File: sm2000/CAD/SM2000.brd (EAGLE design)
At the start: 160 x 100 mm, 365 parts, among them CN1 HDR100-3, CN10 ST-3509, CN11 HDR100-3, CN2 JS-MU3-002, CN3 DS-0518, CN5 ST-3509, CN8 ST-3509, J1 JMP-2PIN, J2 JMP-2PIN, J3 JMP-2PIN, J4 CONN-BOOM-XH-2A, P10 TPAD50, P11 TPAD50, P12 TPAD50, P13 TPAD50, P14 TPAD50, P16 TPAD50, P18 TPAD50, P19 TPAD50, P20 TPAD50, P21 TPAD50, P3 TPAD50, P4 TPAD50, P5 TPAD50, P6 TPAD50, P7 TPAD50, P8 TPAD50, P9 TPAD50, Q1 MMBT3904, Q10 MMBT3904, Q11 STR2P3LLH6, Q12 BRF92, Q13 BFQ19, Q14 RD01MUS2, Q15 MMBT3904, Q17 MMBT3904, Q18 MMBT3904, Q2 MMBT3904, Q3 MMBT3904, Q4 MMBT3904, Q5 MMBT3904, Q6 MMBT3904, Q7 BC548, Q8 BC549, Q9 STR2P3LLH6, SW1 SW-LC2259, SW2 TS-026, SW3 SW-LC2259EENP, SW4 TS-026, SW5 TS-02B, U1 STM32F405VGT6, U10 DNL, U11 L78MXX, U12 PGA-103+, U13 ADE-1, U14 SI570, U15 SI5351A, U2 L78MXX, U3 STMPS2141, U4 EMIF02-USB03F2, U5 L78MXX, U6 LD3985M33R, U7 SA612A, U8 LM386M-1, U9 LMV341, X1 BU-SMA-H, X2 BU-SMA-H

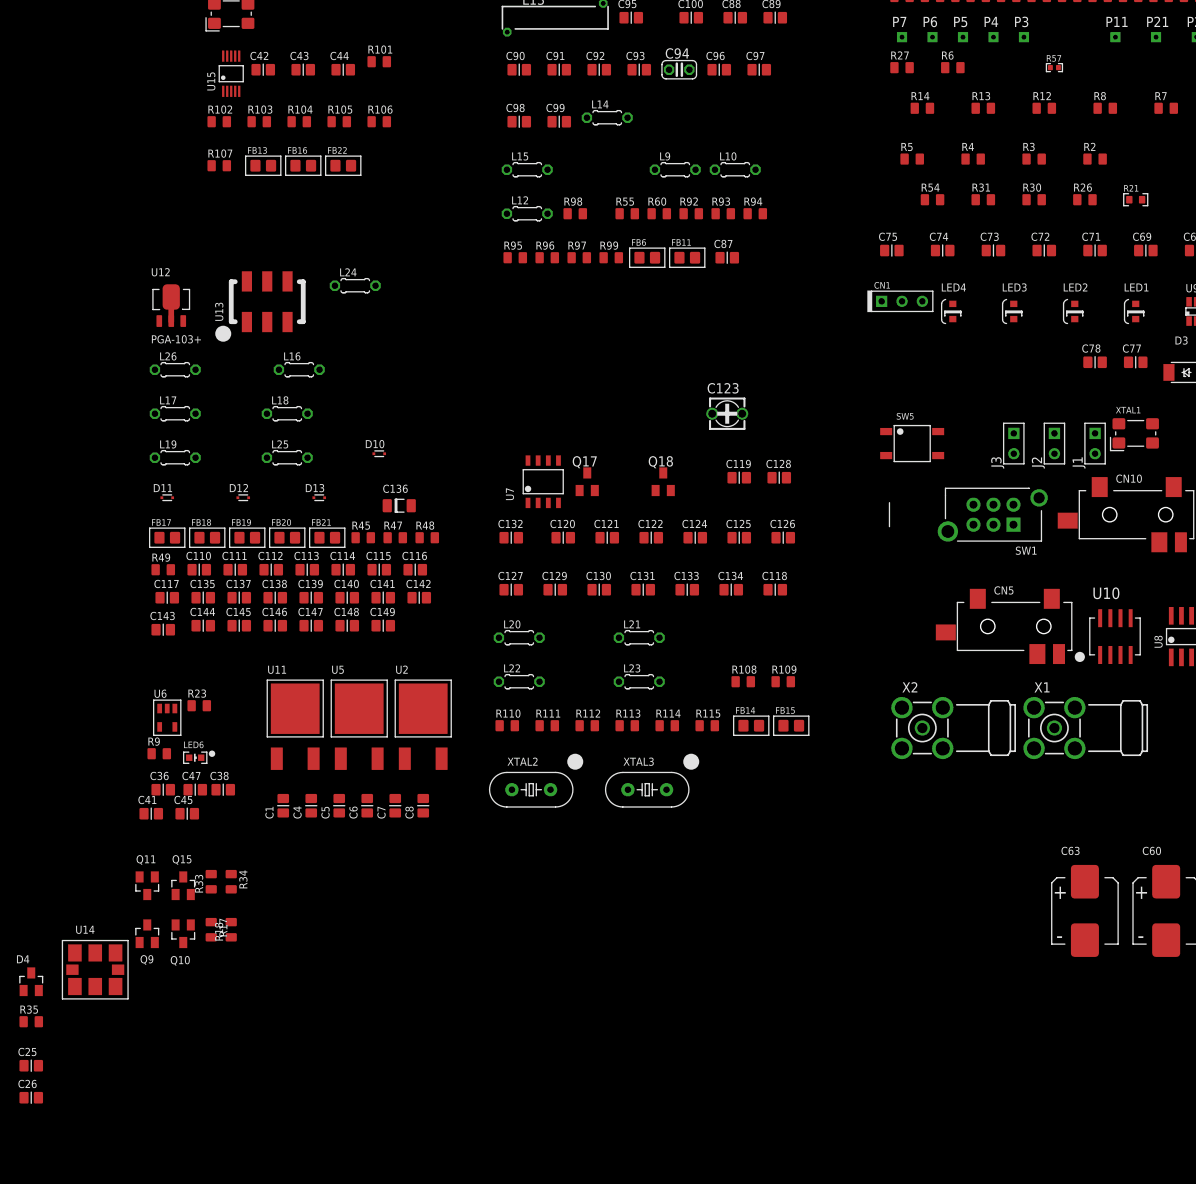
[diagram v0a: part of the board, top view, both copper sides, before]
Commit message: Intermediate update: Fix resistor tolerances fix cap working voltages Fix some library items for no name & no value email Schematic Updates 01/01/2016 item 1. email Commits to SVN 01/02/2016 items 1, i,ii,iii,iv, 2,3,4 RGB
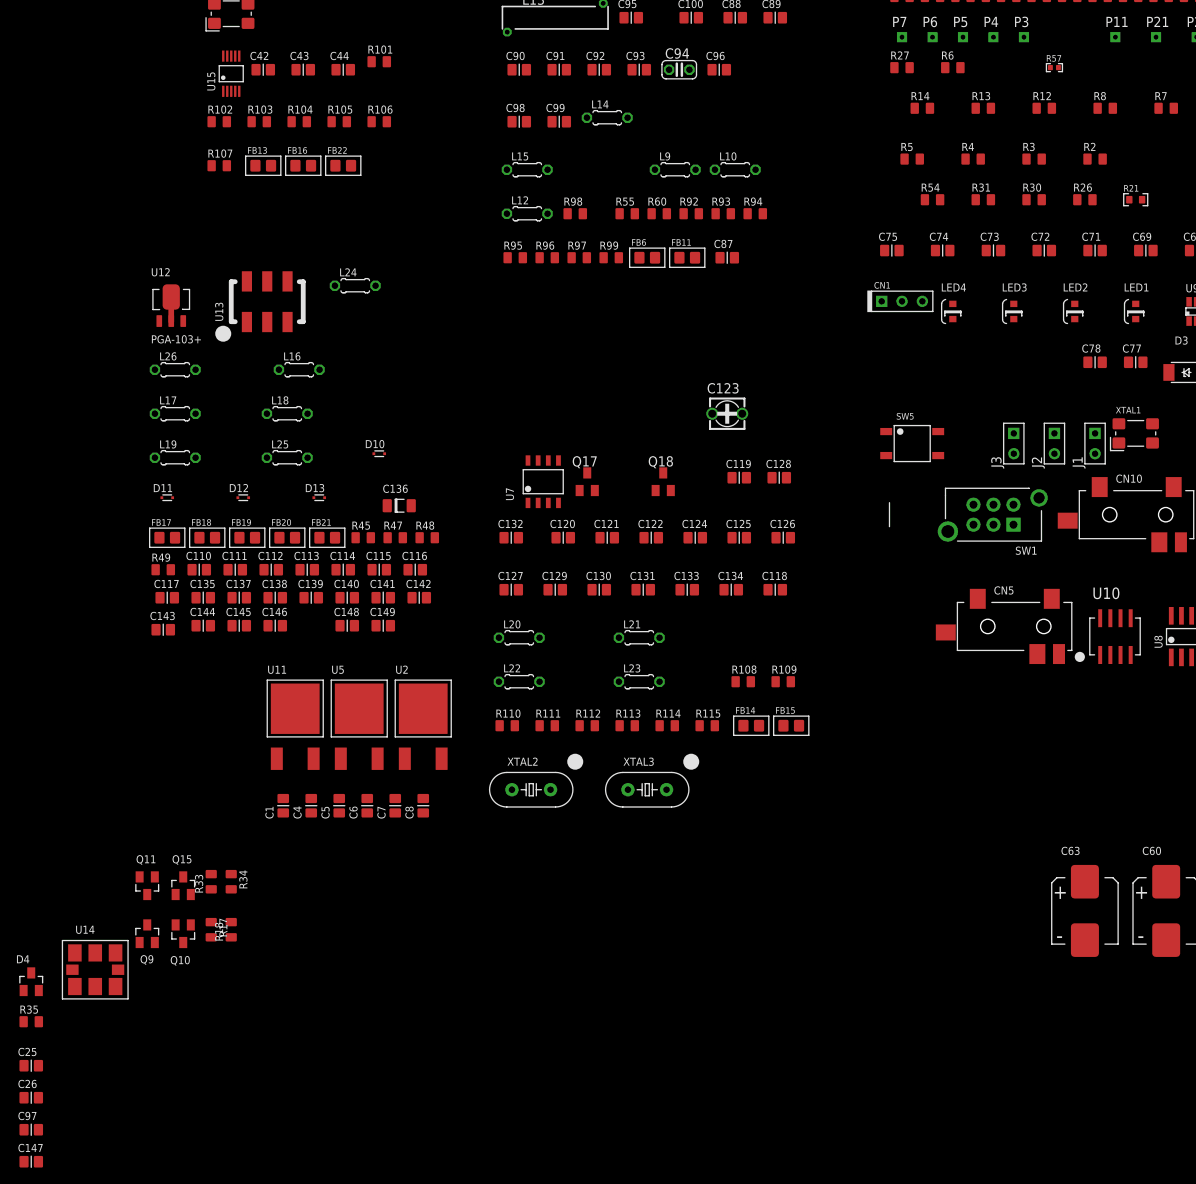
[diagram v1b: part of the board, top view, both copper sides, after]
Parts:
- removed C36, C47: 1uF,16V, _RoweTel:C0805
- removed C38: 10nF,25V, _RoweTel:C0805
- removed C41, C45: 100nF,25V, _RoweTel:C0805
- removed LED6: DNL, _RoweTel:SML-LX0603SRW
- removed R23: 0 Ohm, _RoweTel:R0805
- removed R9: DNL, _RoweTel:R0805
- removed U6: LD3985M33R, _RoweTel:SOT23-5L
- removed X1, X2: BU-SMA-H, _RoweTel:BU-SMA-H
- C100, C93: value 33p -> 33pF,50V
- C110: value 12p -> 12pF.50V
- C111, C112, C139, C140: value 3p3 -> 3.3pF,50V
- C113, C138, C141: value 12p -> 12pF,50V
- C114, C142: value 0.5p -> 0.5pF,50V
- C115, C116, C117, C130, C133, C134, C135, C137, C147, C148, C149, C88, C90, C96, C98: value 1n -> 1nF,25V
- C118, C121, C124, C125, C126, C131, C78: value 0.1u -> 0.1uF,25V
- C120: value 39pF -> 39pF,50V
- C122, C89: value 5p6 -> 5.6pF,50V
- C127: value 27pF -> 27pF,50V
- C128, C132: value 150pF -> 150pF,50V
- C129, C91, C92, C97: value 0.1u -> 0.1uF.25V
- C136: value 1u -> 1uF,25V
- C143, C144: value 2p2 -> 2.2pF,50V
- C145, C94: value 22p -> 22pF,50V
- C146: value 22p -> 22pF,25V
- C25: value (none) -> 1pF,50V
- C26: value (none) -> 1nF,25V
- C28: value 100nF -> 100nF,25V
- C87: value 22pF -> 22pF,50V
- C95: value 1n DNL -> 1nF,25V
- C99: value 47p -> 47pF,50V
- L14, L15: value 57nH air core 4T 2mm ID -> 57nH
- L16, L17, L18, L19: value 68nH 4.5T 5mm ID -> 68nH
- L24: value 260nH 8T 6.25mm ID -> 260nH
- L26: value 220nH 7T 6.25mm ID -> 220nH
- Q7: value BC548 -> MMBT3904
- Q8: value BC549 -> MMBT3906
- R101, R104, R115, R92: value 150 -> 150,1%
- R102, R103, R109, R113, R84, R94: value 1k -> 1K,1%
- R105, R106, R107: value 0R -> 0 Ohm
- R108, R60, R93: value 3k -> 3K,1%
- R110, R70, R80, R86, R87, R96, R97: value 10 -> 10,1%
- R111: value 33k -> 33K,1%
- R112: value 15k -> 15K,1%
- R114: value 50 -> 50,1%
- R35: value RES-0805 -> 330,1%
- R45, R47, R83: value 18k -> 18K,1%
- R48: value 68k -> 68K,1%
- R49, R88: value 2k2 -> 2.2K,1%
- R55: value 10k -> 10K,1%
- R59, R72: value 330 -> 330,1%
- R63, R73: value 680 -> 680,1%
- R64, R74: value 10K -> 10K,1%
- R65, R68, R75, R78: value 2.2K -> 2.2K,1%
- R66, R76: value 180 -> 180,1%
- R67, R77: value 15 -> 15,1%
- R69, R79: value 470 -> 470,1%
- R71, R81: value 47 -> 47,1%
- R82: value 39k -> 39K,1%
- R85, R91: value 3k3 -> 3.3K,1%
- R89, R90: value 100 -> 100,1%
- R95: value 50 -> 49.4,1%
- R98: value 47 DNL -> 47,1%, DNL
- R99: value 4k7 -> 4.7K,1%
- moved C97 160.7 mm to (-228.0, -38.0)
- moved C147 75.6 mm to (-228.0, -42.0)
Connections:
- net N$38 renamed DRIVER/PA_INPUT
- removed net N$100: C71.2, C75.1, X1.1
- removed net N$37 (its old number): C38.1, U6.4
- removed net N$40: Q11.3, R80.1
- removed net N$52: LED6.A, R9.1
- removed net N$56: L20.1
- removed net N$79: L11.2, L13.2, R97.1
- removed net N$90: C69.1, C76.2, X2.1
- new net N$19: L13.1, R97.1
- new net PA_OUTPUT: C149.2
- new net RX+12V: Q9.3, R70.2
- new net TIAIN: C71.2, C75.1, U13.5
- new net TIAOUT: C69.1, C76.2, L20.1
- new net TX+12V: L11.2, Q11.3, R47.1, R49.2, R80.1
- net +12V: no longer Q11.2, Q9.2, R17.2, R33.2
- net +12V_RX: now also R45.1; no longer Q9.3, R70.2
- net +3.3V: no longer C36.1, C41.1, R23.1, R9.2, U6.5
- net +5V: no longer C45.1, C47.1, U6.1, U6.3
- net +9V: now also L13.2; no longer L13.1
- net +VIN: now also Q11.2, Q9.2, R17.2, R33.2
- net GND: no longer C36.2, C38.2, C41.2, C45.2, C47.2, LED6.C, U6.2, X1.2, X1.3, X1.4, X1.5, X2.2, X2.3, X2.4, X2.5
- net VDD: no longer R23.2

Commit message: Update schematic. Moved new component footprints onto PCB Matched schematic to emailchange lists. reorganized circuitry blocks on pages. RGB
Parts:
- added C27: 1nF,25V, _RoweTel:C0805
- added J10, J11, J12, J5, J6, J7, J8, J9: JMPR-2X2, _RoweTel:JMPR-2X2X.1
- added SH4, SH5: SHUNT, _RoweTel:SHUNT
- C119, C80, C81: value 10uF -> 10uF,25V,EL; device _RoweTel:C0805 -> _RoweTel:NICHICON-WJ-5
- C79, C82: value 10uF tant -> 10uF,25V,EL; device _RoweTel:C0805 -> _RoweTel:NICHICON-WJ-5
- R114: value 50,1% -> 49.9,1%
- R95: value 49.4,1% -> 49.9,1%
- moved U14 243.5 mm to (12.0, 56.0)
- moved L19 241.6 mm to (31.5, 53.5)
- moved L17 241.6 mm to (31.5, 57.0)
- moved L26 241.5 mm to (31.5, 60.5)
- moved L25 235.1 mm to (39.0, 53.5)
- moved L18 235.1 mm to (39.0, 57.0)
- moved L16 233.5 mm to (39.0, 60.5)
- moved Q14 224.5 mm to (39.0, 19.0)
- moved L24 219.0 mm to (31.5, 64.0)
- moved XTAL5 215.2 mm to (11.0, 79.0)
- moved U13 210.0 mm to (11.5, 68.5)
- moved L15 205.5 mm to (39.0, 67.5)
- moved L12 205.4 mm to (39.0, 64.0)
- moved U11 204.6 mm to (9.50, 17.0)
- moved U2 204.6 mm to (25.5, 17.0)
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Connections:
- net +12V_RX_ENB renamed +12VRXENB
- removed net N$127: C111.2, U13.3
- new net N$40: C126.2, J6.1
- new net N$52: C100.1, J9.1, L14.2
- new net N$56: C111.2, J12.2
- new net N$58: J12.1, U13.3
- new net N$59: C27.2, J10.1
- new net N$61: C27.1, U12.1
- new net N$63: J8.1
- new net N$79: C112.1, J11.1
- new net TIA_OUT: C69.1, C76.2, J5.1, L20.1
- net ANT_SMA: now also J9.2; no longer C100.1, L14.2
- net BBAMP: now also J7.1
- net GND: now also J10.3, J10.4, J11.3, J11.4, J12.3, J12.4, J5.3, J5.4, J6.3, J6.4, J7.3, J7.4, J8.3, J8.4, J9.3, J9.4
- net N$104: now also J7.2
- net N$11: now also J10.2; no longer U12.1
- net N$112: now also J8.2
- net N$135: now also J11.2; no longer C112.1
- net N$49: now also J6.2; no longer C126.2
- net TIAOUT: now also J5.2; no longer C69.1, C76.2, L20.1

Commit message: Implemented changes from D. Rowes email: Comments #1 RGB
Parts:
- removed C64: 22uF,25V, _RoweTel:C0805
- removed C66: 100nF,25V, _RoweTel:C0805
- removed U5: L78MXX, _RoweTel:DPAK
- added C101: 10nF,25V, _RoweTel:C0805
- added C103, C164: 100nF,25V, _RoweTel:C0805
- added C107: 100nF,25V, AA-ipc-7351-capacitor:CAPC1005X60N
- added C108: 20pF,50V, AA-ipc-7351-capacitor:CAPC1005X60N
- added C109: 8.2nF,25V, ipc-7351-capacitor:CAPC1608X92N
- added C150, C179: 22uF,25V, _RoweTel:C1210
- added C166: 470nF,25V, ipc-7351-capacitor:CAPC1608X92N
- added C167: 22uF,25V,1210, AA-ipc-7351-capacitor:CAPC3225X168N
- added C29, C31: CAP-10UF-WJ5, _RoweTel:NICHICON-WJ-5
- added C36: 1nF,25V, _RoweTel:C0805
- added J13: JMPR-2X2, _RoweTel:JMPR-2X2X.1
- added L1: 4.2uH, _RoweTel:SRR5028
- added R127: 124.0K,1%, AA-ipc-7351-resistor:RESC1005X40AN
- added R128: 22.1K,1%, AA-ipc-7351-resistor:RESC1005X40AN
- added R129: 10K,1%, AA-ipc-7351-resistor:RESC1005X40AN
- added U$16: (no value), _RoweTel:SWPS-OTL
- added U17: TPS54329E, _RoweTel:PSO-DDA
- added U6: LD3985M33R, _RoweTel:SOT23-5L
- C1: value .33uF,25V -> 100nF,25V
- C5, C7: value .33uF,25V -> CAP-10UF-WJ5; device _RoweTel:C0805 -> _RoweTel:NICHICON-WJ-5
- C65: value 1uF,16V -> 1uF,25V
- moved C1 247.8 mm to (50.0, -23.0), turned to 0 degrees
- moved C147 44.6 mm to (-224.5, 2.50)
- moved C25 44.6 mm to (-224.5, 14.5)
- moved C26 44.6 mm to (-224.5, 10.5)
- moved C97 44.6 mm to (-224.5, 6.50)
- moved D4 44.6 mm to (-224.5, 25.0)
- moved R35 44.6 mm to (-224.5, 20.0)
- moved C27 23.3 mm to (-224.5, -1.50)
- moved C7 21.8 mm to (-201.0, 14.0), turned to 0 degrees
- moved C5 12.3 mm to (-185.0, 14.0), turned to 0 degrees
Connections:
- removed net N$63: J8.1
- new net N$127: C101.1, U6.4
- new net N$169: C107.1, U17.1
- new net N$170: C108.2, R127.2, R128.1, U17.5
- new net N$171: C109.1, U17.8
- new net N$172: C166.1, U17.6
- new net N$173: R129.2, U17.7
- new net N$222: C150.1, C164.1, C179.1, C36.1, R129.1, R21.2, U17.2
- new net N$90: J13.2, U13.5
- new net SW: C107.2, L1.1, U17.3
- net +3.3V: now also C8.1, U11.3
- net +5V: now also C108.1, C167.1, C7.1, FB8.1, L1.2, R127.1, U11.1; no longer C6.1, U5.3
- net +9V: now also L11.2; no longer L13.2
- net +VIN: now also C31.1, U2.1
- net AVDD: now also C5.1, C6.1, FB7.1, U6.5; no longer C64.1, C66.1, FB8.2
- net GND: now also C101.2, C103.2, C109.2, C150.2, C164.2, C166.2, C167.2, C179.2, C29.2, C31.2, C36.2, J13.3, J13.4, R128.2, U17.4, U17.EP, U6.2; no longer C64.2, C66.2, U5.4
- net N$144: now also XTAL3.2; no longer XTAL3.1
- net N$145: now also XTAL3.1; no longer XTAL3.2
- net N$54: now also C103.1, C29.1, FB8.2, U6.1, U6.3; no longer C5.1, C7.1, R21.2, U11.1, U2.1, U5.1
- net TIAIN: now also J13.1; no longer U13.5
- net TX+12V: now also L13.2; no longer L11.2
- net VDD: no longer C8.1, FB7.1, FB8.1, U11.3
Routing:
- added copper zone on layer 15, net AVDD
- added copper zone on layer 2, net GND
- added copper zone on layer 15, net VDD
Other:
- board text added: "L2-GND"
- board text added: "L3-VDD-AVDD"

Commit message: Changes to schematics per emails of 1/12/2016 - 1/14/2016 per David Rowe.
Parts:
- removed C101: 10nF,25V, _RoweTel:C0805
- removed P5, P6, P7, P8: TPAD50, _Coherix:TPAD50
- removed U$16: (no value), _RoweTel:SWPS-OTL
- added C38: 100uF,25V,EL, _RoweTel:CAP-CHEMI-F80
- added C41: 0.1uF.25V, _RoweTel:C0805
- added J14: HDR100-5, _RoweTel:HDR100-5
- added L2: RFC, _RoweTel:Z15/4
- added LED10, LED11, LED5, LED6, LED7: SML-LX0603GW, _RoweTel:SML-LX0603SRW
- added LED8: SML-LX0603SRW, _RoweTel:SML-LX0603SRW
- added LED9: SML-LX0603YW, _RoweTel:SML-LX0603SRW
- added R100, R52: 1K,1%, _RoweTel:R0805
- added R116: 680,1%, _RoweTel:R0805
- added R117, R44, R51: 320,1%, _RoweTel:R0805
- added R23, R43, R9: 10K,1%, _RoweTel:R0805
- added R36: 1.5K,1%, _RoweTel:R0805
- added U5: LMV341, _RoweTel:SOT23-6
- added X1: BU-SMA-H, _RoweTel:BU-SMA-H
- C1: value 100nF,25V -> 22uF,25V; device _RoweTel:C0805 -> _RoweTel:C1210
- C103: value 100nF,25V -> 1nF,25V
- C136: value 1uF,25V -> 1uF,25V,EL
- C29: value CAP-10UF-WJ5 -> 1nF,25V; device _RoweTel:NICHICON-WJ-5 -> _RoweTel:C0805
- C5: value CAP-10UF-WJ5 -> 0.1uF.25V; device _RoweTel:NICHICON-WJ-5 -> _RoweTel:C0805
- C94: device rcl:C025-024X044 -> _RoweTel:C0805
- L10, L12, L14, L15, L16, L17, L18, L19, L25, L26, L9: device rcl:0204/5 -> _RoweTel:L10X15
- L11, L13: device inductor-neosid:Z15/4 -> _RoweTel:Z15/4
- L20, L21, L22, L23: device rcl:0204/5 -> _RoweTel:L-TDK-MLF2012
- Q12: device transistor:SOT23-EBC -> _RoweTel:SOT23
- Q13: device transistor:SOT23-EBC -> _RoweTel:SOT89
- R18, R34: value 10K,1/8W,5% -> 10K,1%
- R61, R62: value DNL -> 4.7K,1%
- U6: value LD3985M33R -> AP7215Y-33; device _RoweTel:SOT23-5L -> _RoweTel:SOT89
- moved L20 308.1 mm to (127.5, 114.0), turned to 270 degrees
- moved L22 307.7 mm to (127.5, 107.0), turned to 270 degrees
- moved L21 299.0 mm to (133.0, 114.0), turned to 270 degrees
- moved L23 298.6 mm to (133.0, 107.0), turned to 270 degrees
- moved CN5 244.5 mm to (138.8, 8.91)
- moved CN10 209.4 mm to (117.6, 10.4)
- moved SW1 203.4 mm to (93.8, 10.9)
- moved CN2 195.1 mm to (150.2, 42.7), turned to 270 degrees
- moved CN8 193.2 mm to (138.1, 22.9)
- moved C29 167.0 mm to (-30.0, -22.5), turned to 90 degrees
- moved U6 157.9 mm to (-77.5, -21.0), turned to 90 degrees
- moved C5 155.3 mm to (-34.0, -22.5), turned to 90 degrees
- moved L13 148.3 mm to (147.5, 110.5), turned to 270 degrees
- moved L11 143.9 mm to (140.0, 110.5), turned to 90 degrees
- moved SW3 115.9 mm to (93.7, 22.3)
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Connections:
- net TXDAC renamed TX_DAC
- removed net +12V: FB10.2, FB14.2, FB15.1
- removed net +12V_RX: R45.1
- removed net +3.3V: C8.1, FB13.1, FB16.1, FB22.1, U11.3
- removed net AVDD: C22.1, C35.1, C5.1, C6.1, C65.1, FB7.1, J3.2, R38.2, U6.5, U9.5, U9.6
- removed net SCL: U14.8, U15.4
- removed net SDA: U14.7, U15.5
- removed net VDD: C16.1, C17.1, C18.1, C19.1, C20.1, C21.1, C52.1, C53.1, P13.1, R2.1, R24.1, R25.2, R3.1, R31.1, R37.1, R4.1, R5.1, R61.1, R62.1, R7.2, R8.2, SW1.2, SW1.5, U1.100, U1.11, U1.19, U1.28, U1.50, U1.75, U10.8
- new net +12VTXENB: R18.1
- new net 3V3: C16.1, C17.1, C18.1, C19.1, C20.1, C21.1, C52.1, C53.1, C8.1, FB13.1, FB16.1, FB22.1, P13.1, R2.1, R24.1, R25.2, R3.1, R31.1, R37.1, R4.1, R44.2, R5.1, R61.1, R62.1, R7.2, R8.2, SW1.2, SW1.5, U1.100, U1.11, U1.19, U1.28, U1.50, U1.75, U10.8, U11.3
- new net A3V3: C22.1, C35.1, C6.1, C65.1, FB21.2, FB7.1, J3.2, R38.2, R51.2, U5.5, U5.6, U6.3, U9.5, U9.6
- new net N$128: R43.1, R9.1, U5.3
- new net N$129: J8.1
- new net N$130: C29.1, C5.1, L11.1, L2.1
- new net N$131: LED8.A, R52.1
- new net N$132: LED6.A, R44.1
- new net N$134: LED10.A, R116.1
- new net N$138: LED11.A, R117.1
- new net N$63: LED5.A, R36.1
- new net VGG_DAC: U5.1
- net +12VRXENB: no longer R18.1
- net +5V: now also FB10.2, FB14.2, FB15.1, R116.2
- net +9V: now also C38.1, C41.1, L2.2, R36.2; no longer L11.2
- net +VIN: now also R117.2
- net ANT_SMA: now also X1.1; no longer J9.2
- net BBAMP: now also L23.P$2; no longer L23.2
- net GND: now also C38.2, C41.2, J14.1, L21.P$1, LED10.C, LED11.C, LED5.C, LED6.C, LED7.C, LED8.C, LED9.C, R23.1, R43.2, U5.2, U6.1; no longer C101.2, L21.1, U6.2
- net N$127: now also LED7.A, R51.1; no longer C101.1, U6.4
- net N$133: now also LED9.A, R100.1; no longer FB21.2
- net N$143: now also L20.P$2; no longer L20.2
- net N$145: now also L21.P$2; no longer L21.2
- net N$151: now also L22.P$1; no longer L22.1
- net N$156: now also L23.P$1; no longer L23.1
- net N$158: now also R23.2
- net N$19: now also L13.2; no longer L13.1
- net N$32: now also L11.2; no longer L11.1
- net N$51: now also L22.P$2; no longer L22.2
- net N$54: now also U6.2; no longer C29.1, U6.1, U6.3
- net N$70: now also Q12.2; no longer Q12.E
- net N$71: now also Q13.3; no longer Q13.E
- net N$75: now also Q13.1; no longer Q13.B
- net N$78: now also Q12.1; no longer Q12.B
- net N$82: now also Q12.3; no longer Q12.C
- net N$84: now also Q13.2, Q13.2.1; no longer Q13.C
- net PA_OUTPUT: now also J9.2
- net PE0: now also J14.2; no longer P5.1
- net PE1: now also J14.3; no longer P6.1
- net PE2: now also J14.4; no longer P7.1
- net PE3: now also J14.5; no longer P8.1
- net RX+12V: now also R45.1, R52.2
- net SCL3: now also U14.8, U15.4
- net SDA3: now also U14.7, U15.5
- net TIAOUT: now also L20.P$1
- net TIA_OUT: no longer L20.1
- net TX+12V: now also L13.1, R100.2; no longer L13.2
- net VGG: now also R9.2, U5.4
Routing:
- removed copper zone on layer 15, net AVDD
- removed copper zone on layer 2, net GND
- removed copper zone on layer 15, net VDD
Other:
- board text removed: "L2-GND"
- board text removed: "L3-VDD-AVDD"
